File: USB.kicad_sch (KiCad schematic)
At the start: 44 parts, among them J3 USB_C_Receptacle_USB2.0, J4 USB_A_Stacked, U2 CP2102N-Axx-xQFN20, U3 FSUSB42MUX, U4 FSUSB42MUX, U5 TPD4EUSB30, U6 USB2422, U7 AP2171W, U8 TPD4EUSB30, Y1 24MHz

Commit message: Use HRO USB-C part number to match footprint
The footprint is not compatible with the JAE part. Specify the HRO USB-C
part number instead.

Fixes: #14

Signed-off-by: Stefan Agner <stefan@agner.ch>
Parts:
- J3: Manufacturer JAE -> HRO; PartNumber DX07S016JA3R1500 -> TYPE-C-31-M-12
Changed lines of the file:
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@@
       (effects (font (size 1.27 1.27)) hide)
     )
-    (property "Manufacturer" "JAE" (id 4) (at 153.67 140.97 0)
+    (property "Manufacturer" "HRO" (id 4) (at 153.67 140.97 0)
       (effects (font (size 1.27 1.27)) hide)
     )
-    (property "PartNumber" "DX07S016JA3R1500" (id 5) (at 153.67 140.97 0)
+    (property "PartNumber" "TYPE-C-31-M-12" (id 5) (at 153.67 140.97 0)
       (effects (font (size 1.27 1.27)) hide)
     )

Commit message: Fix CP2102N footprint
Choose Silicon Labs specific QFN20 footprint.

Signed-off-by: Stefan Agner <stefan@agner.ch>
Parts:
- U2: footprint Package_DFN_QFN:SiliconLabs_QFN-20-1EP_3x3mm_P0.5mm -> Package_DFN_QFN:SiliconLabs_QFN-20-1EP_3x3mm_P0.5mm_EP1.8x1.8mm
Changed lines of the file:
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@@
     (property "Reference" "U2" (id 0) (at 35.56 160.655 0))
     (property "Value" "CP2102N-Axx-xQFN20" (id 1) (at 58.42 160.655 0))
-    (property "Footprint" "Package_DFN_QFN:SiliconLabs_QFN-20-1EP_3x3mm_P0.5mm" (id 2) (at 77.47 160.655 0)
+    (property "Footprint" "Package_DFN_QFN:SiliconLabs_QFN-20-1EP_3x3mm_P0.5mm_EP1.8x1.8mm" (id 2) (at 77.47 160.655 0)
       (effects (font (size 1.27 1.27)) hide)
     )

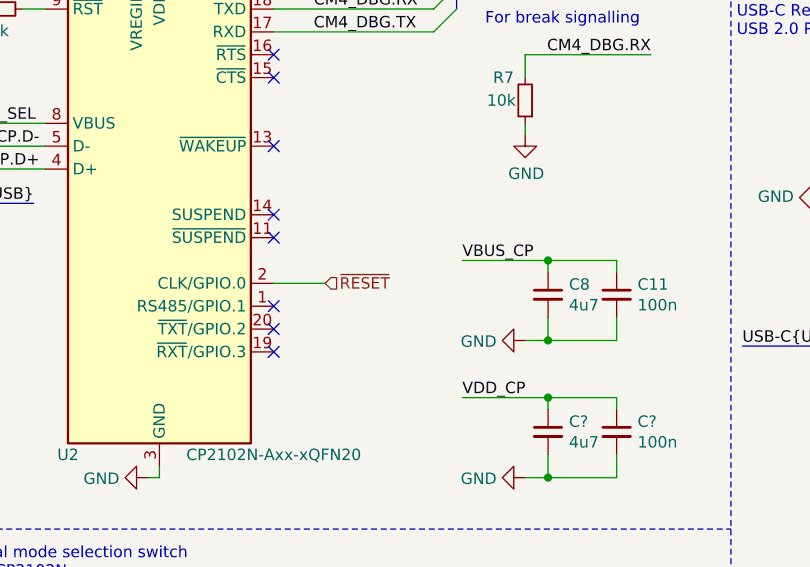
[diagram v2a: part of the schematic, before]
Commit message: Redesign buttons/switches
Remove power/reset/recovery switch. Power and reset is not really required
and recovery mode (USB Boot) can be triggered via jumper. Make the Fan
and RPiLED a new separate config so we can leave them unpopulated. Add a
second GPIO controlled switch.

Fixes: #16

Signed-off-by: Stefan Agner <stefan@agner.ch>
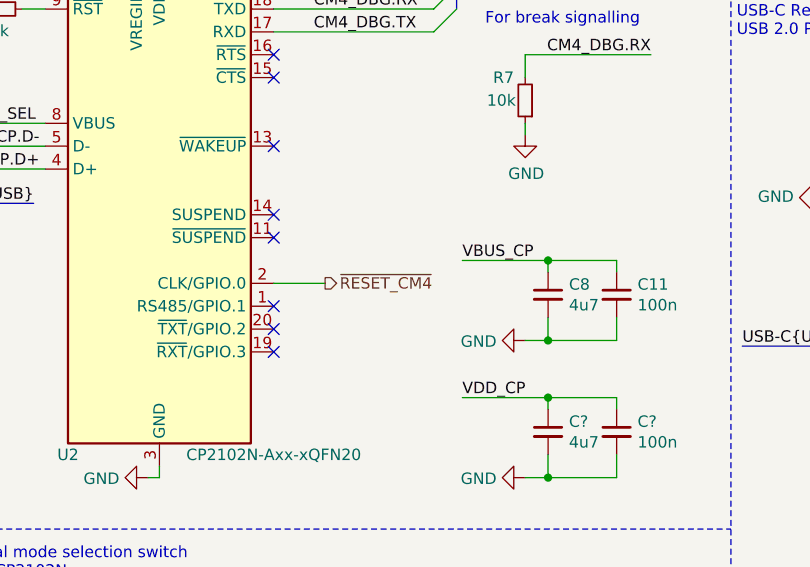
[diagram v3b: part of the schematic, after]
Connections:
- net ~RESET renamed ~RESET_CM4
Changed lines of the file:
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@@
     (comment 2 "Light Blue")
   )
+  (bus_alias "I2C" (members "SDA" "SCL"))
+  (bus_alias "USB" (members "D+" "D-"))
   (bus_alias "CM4_USB" (members "CM4_USB_D+" "CM4_USB_D-" "CM4_USB_OTG_ID"))
-  (bus_alias "USB" (members "D+" "D-"))
-  (bus_alias "I2C" (members "SDA" "SCL"))
   (junction (at 22.86 80.01) (diameter 0.9144) (color 0 0 0 0))
   (junction (at 22.86 88.9) (diameter 0.9144) (color 0 0 0 0))
@@
     (effects (font (size 1.27 1.27)) (justify right))
   )
-  (hierarchical_label "~RESET" (shape input) (at 64.135 141.605 0)
+  (hierarchical_label "~RESET_CM4" (shape output) (at 64.135 141.605 0)
     (effects (font (size 1.27 1.27)) (justify left))
   )
@@
   (symbol (lib_id "power:GND") (at 86.36 147.955 270) (unit 1)
     (in_bom yes) (on_board yes)
-    (property "Reference" "#PWR?" (id 0) (at 80.01 147.955 0)
+    (property "Reference" "#PWR0191" (id 0) (at 80.01 147.955 0)
       (effects (font (size 1.27 1.27)) hide)
     )
@@
   (symbol (lib_id "power:GND") (at 86.36 163.195 270) (unit 1)
     (in_bom yes) (on_board yes)
-    (property "Reference" "#PWR?" (id 0) (at 80.01 163.195 0)
+    (property "Reference" "#PWR0192" (id 0) (at 80.01 163.195 0)
       (effects (font (size 1.27 1.27)) hide)
     )
@@
   (symbol (lib_id "power:GND") (at 103.505 75.565 270) (unit 1)
     (in_bom yes) (on_board yes)
-    (property "Reference" "#PWR?" (id 0) (at 97.155 75.565 0)
-      (effects (font (size 1.27 1.27)) hide)
-    )
+    (property "Reference" "#PWR0193" (id 0) (at 97.155 75.565 0)
+      (effects (font (size 1.27 1.27)) hide)
+    )

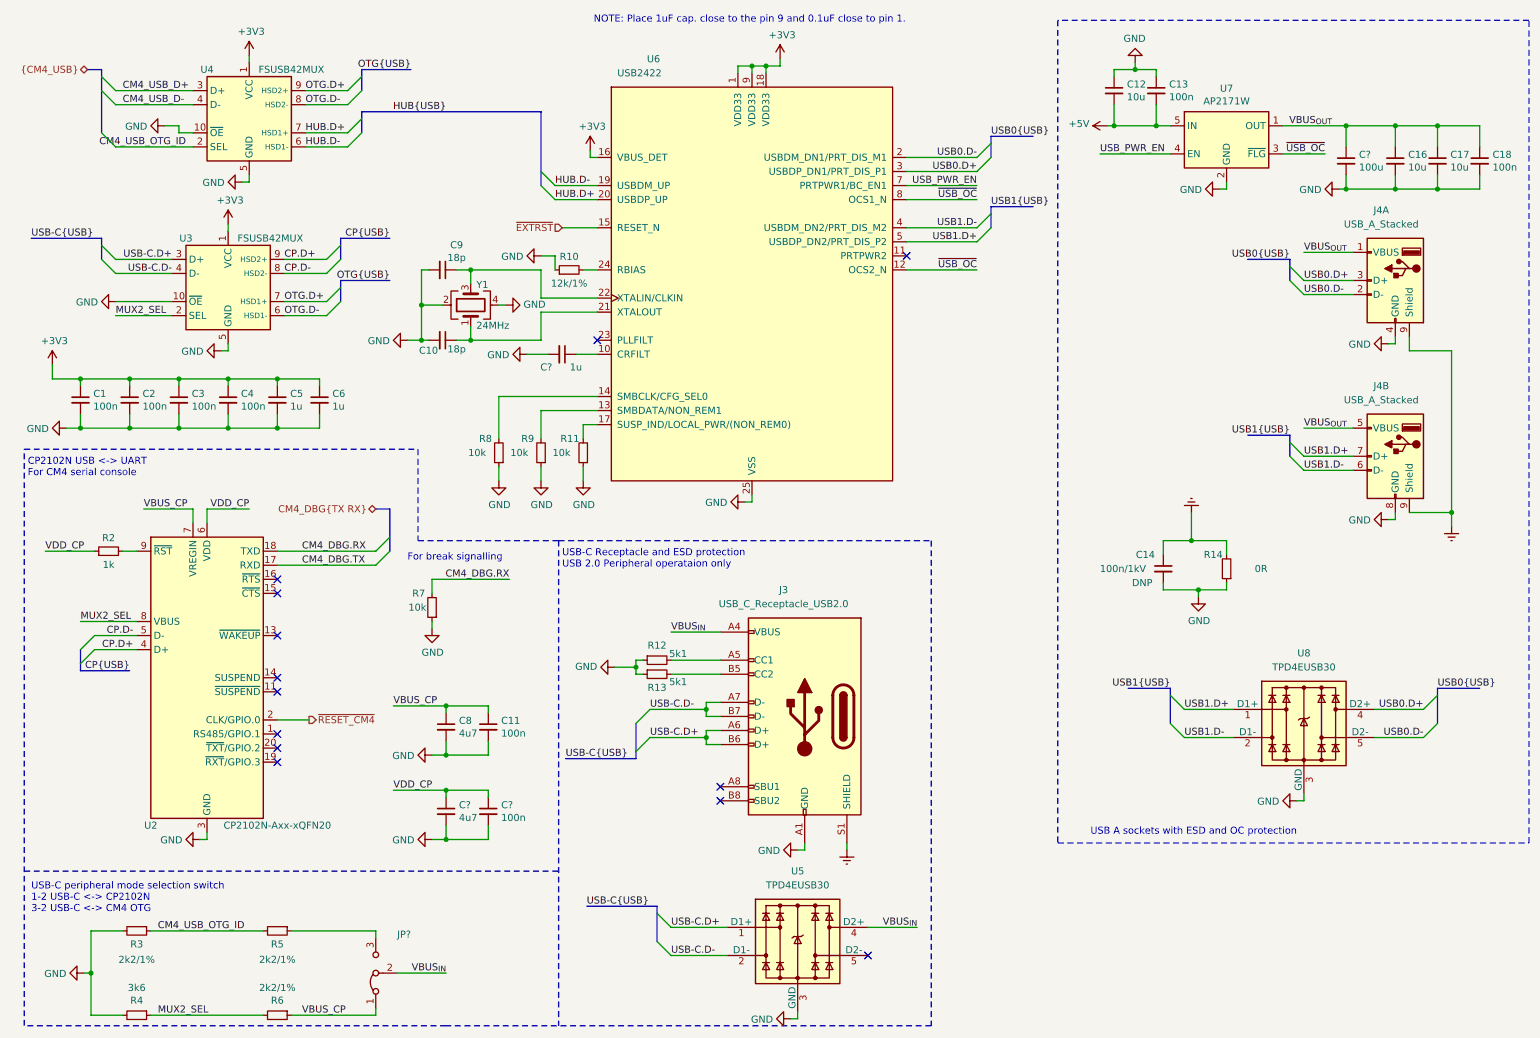
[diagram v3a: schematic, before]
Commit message: Assign footprints and annotate components
Signed-off-by: Stefan Agner <stefan@agner.ch>
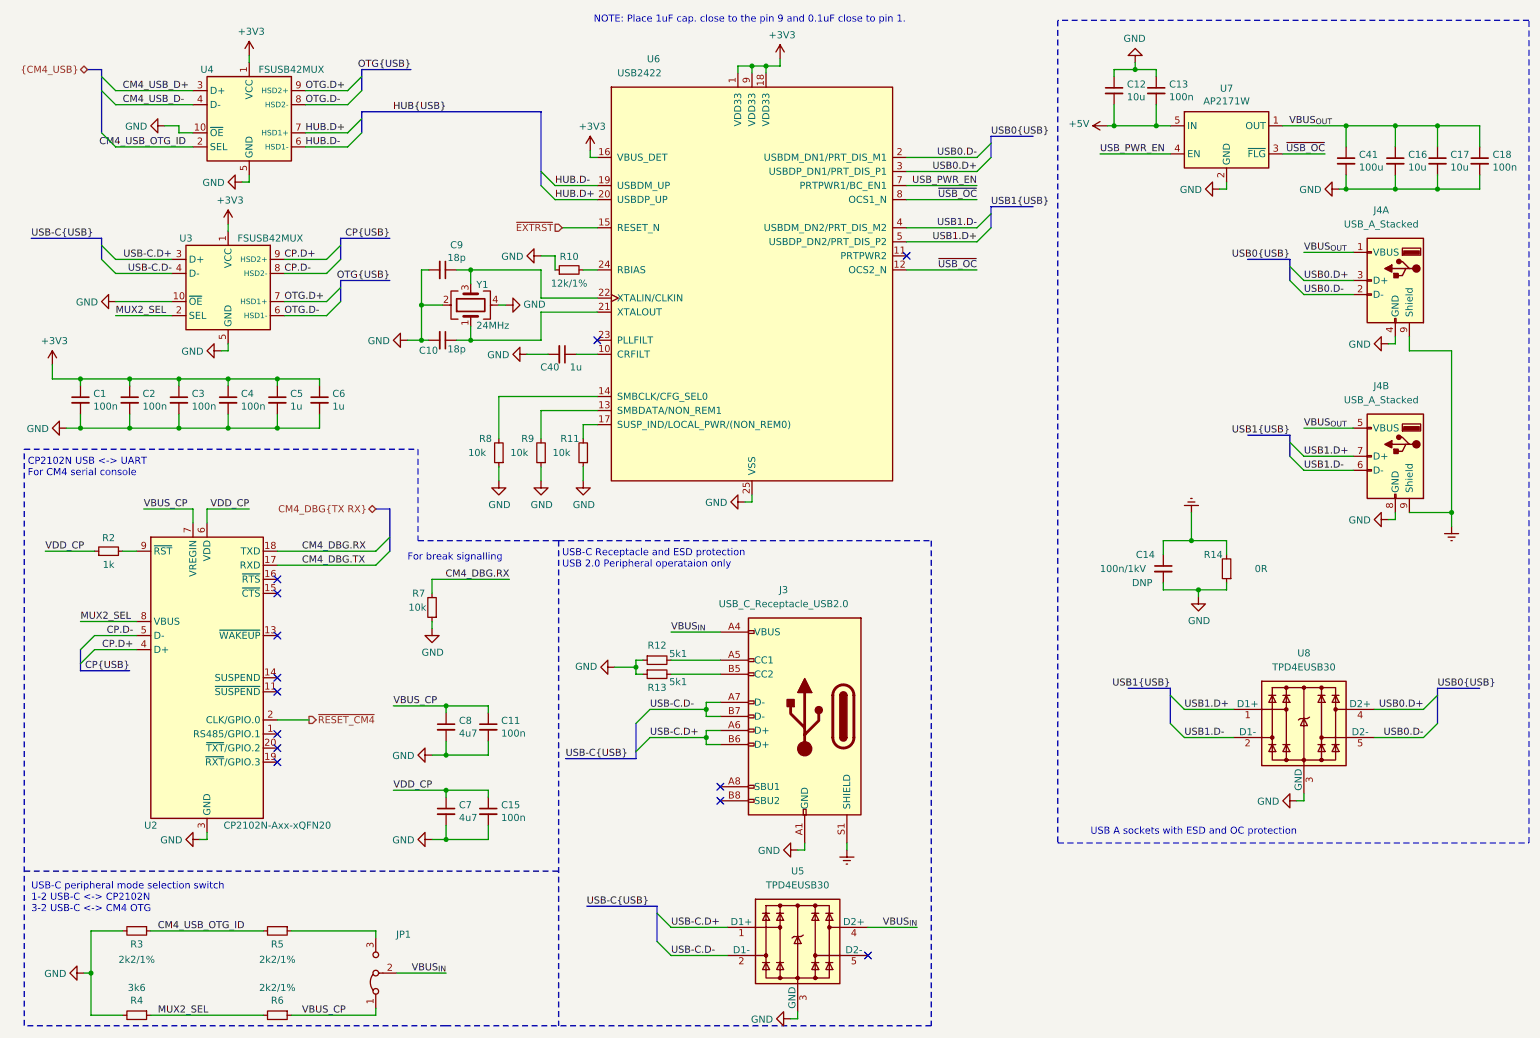
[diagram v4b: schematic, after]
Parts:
- JP1: renamed from JP?; footprint (none) -> Connector_PinHeader_2.54mm:PinHeader_1x03_P2.54mm_Vertical
- gave numbers to parts that had none: 4
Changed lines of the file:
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@@
     (comment 2 "Light Blue")
   )
+  (bus_alias "CM4_USB" (members "CM4_USB_D+" "CM4_USB_D-" "CM4_USB_OTG_ID"))
+  (bus_alias "USB" (members "D+" "D-"))
   (bus_alias "I2C" (members "SDA" "SCL"))
-  (bus_alias "USB" (members "D+" "D-"))
-  (bus_alias "CM4_USB" (members "CM4_USB_D+" "CM4_USB_D-" "CM4_USB_OTG_ID"))
   (junction (at 22.86 80.01) (diameter 0.9144) (color 0 0 0 0))
   (junction (at 22.86 88.9) (diameter 0.9144) (color 0 0 0 0))
@@
   (symbol (lib_id "Device:C_Small") (at 88.9 158.115 0) (unit 1)
     (in_bom yes) (on_board yes)
-    (property "Reference" "C?" (id 0) (at 91.2242 156.9656 0)
+    (property "Reference" "C7" (id 0) (at 91.2242 156.9656 0)
       (effects (font (size 1.27 1.27)) (justify left))
     )
@@
   (symbol (lib_id "Device:C_Small") (at 96.52 158.115 0) (unit 1)
     (in_bom yes) (on_board yes)
-    (property "Reference" "C?" (id 0) (at 98.8442 156.9656 0)
+    (property "Reference" "C15" (id 0) (at 98.8442 156.9656 0)
       (effects (font (size 1.27 1.27)) (justify left))
     )
@@
   (symbol (lib_id "Device:C_Small") (at 109.855 75.565 270) (unit 1)
     (in_bom yes) (on_board yes)
-    (property "Reference" "C?" (id 0) (at 105.9244 77.8892 90)
+    (property "Reference" "C40" (id 0) (at 105.9244 77.8892 90)
       (effects (font (size 1.27 1.27)) (justify left))
     )
@@
   (symbol (lib_id "Device:C_Small") (at 251.46 40.64 0) (unit 1)
     (in_bom yes) (on_board yes)
-    (property "Reference" "C?" (id 0) (at 253.7842 39.4906 0)
+    (property "Reference" "C41" (id 0) (at 253.7842 39.4906 0)
       (effects (font (size 1.27 1.27)) (justify left))
     )
@@
   (symbol (lib_id "Jumper:Jumper_3_Bridged12") (at 76.2 187.325 90) (unit 1)
     (in_bom yes) (on_board yes)
-    (property "Reference" "JP?" (id 0) (at 82.55 180.3399 90)
+    (property "Reference" "JP1" (id 0) (at 82.55 180.3399 90)
       (effects (font (size 1.27 1.27)) (justify left))
     )
@@
       (effects (font (size 1.27 1.27)) (justify left) hide)
     )
-    (property "Footprint" "" (id 2) (at 76.2 187.325 0)
-      (effects (font (size 1.27 1.27)) hide)
-    )
+    (property "Footprint" "Connector_PinHeader_2.54mm:PinHeader_1x03_P2.54mm_Vertical" (id 2) (at 76.2 187.325 0)
+      (effects (font (size 1.27 1.27)) hide)
+    )

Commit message: Adjust Manufacturer/PartNumber for some parts
- Use Diodes B2100-13-F consistently
- Define part for pin headers
- Replace N-Channel MOSFET for PoE with BSZ440N10NS3GATMA1
- Define Input protection MOSFET DMP3013SFV-7

Signed-off-by: Stefan Agner <stefan@agner.ch>
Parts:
- JP1: Manufacturer (none) -> Adam Tech; PartNumber (none) -> PH1-03-UA
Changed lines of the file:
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@@
     (comment 2 "Light Blue")
   )
+  (bus_alias "I2C" (members "SDA" "SCL"))
+  (bus_alias "USB" (members "D+" "D-"))
   (bus_alias "CM4_USB" (members "CM4_USB_D+" "CM4_USB_D-" "CM4_USB_OTG_ID"))
-  (bus_alias "USB" (members "D+" "D-"))
-  (bus_alias "I2C" (members "SDA" "SCL"))
   (junction (at 22.86 80.01) (diameter 0.9144) (color 0 0 0 0))
   (junction (at 22.86 88.9) (diameter 0.9144) (color 0 0 0 0))
@@
       (effects (font (size 1.27 1.27)) hide)
     )
+    (property "Manufacturer" "Adam Tech" (id 4) (at 76.2 187.325 90)
+      (effects (font (size 1.27 1.27)) hide)
+    )
+    (property "PartNumber" "PH1-03-UA" (id 5) (at 76.2 187.325 90)
+      (effects (font (size 1.27 1.27)) hide)
+    )

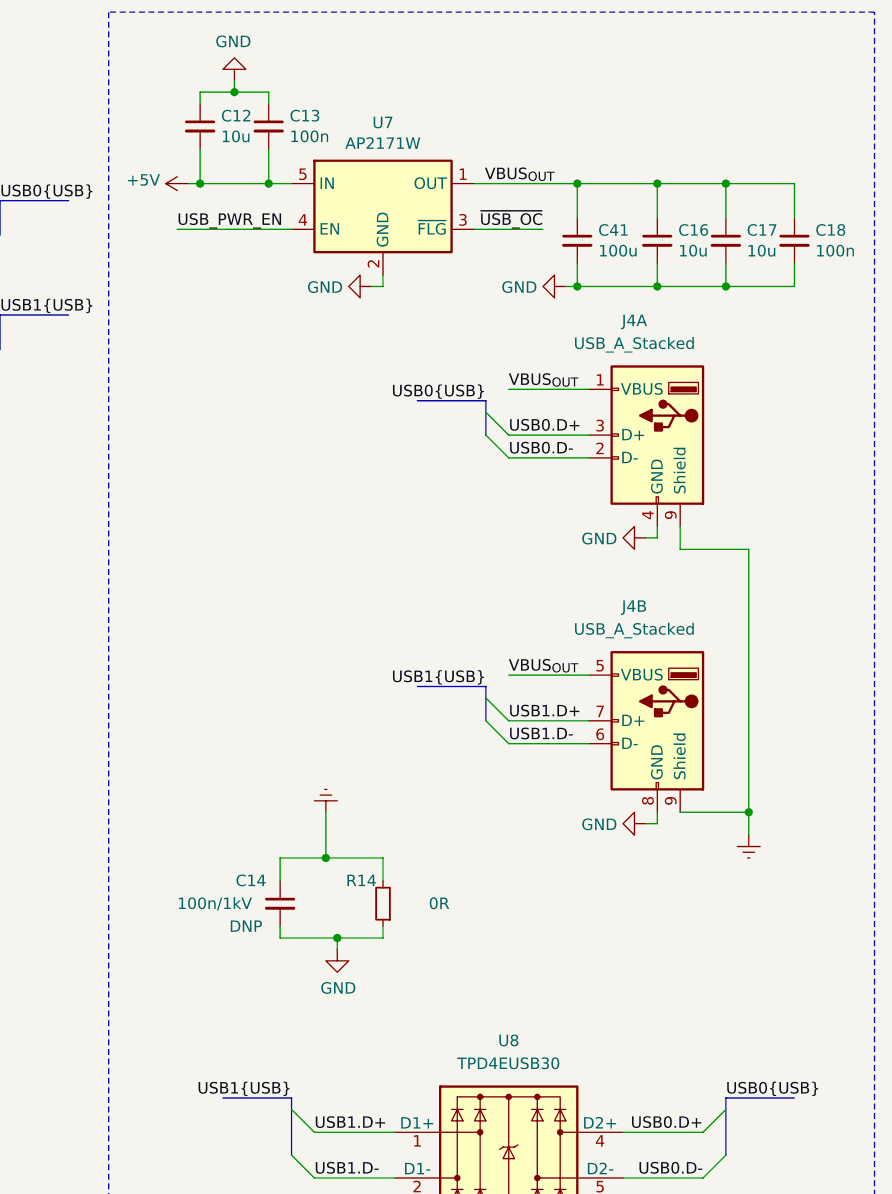
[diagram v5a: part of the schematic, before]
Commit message: Adjust various parts to improve BOM
- Replace unusual/high value ceramics with lower value in parallel
- Use the same protection Shottky Diode in PoE as in regular input
  (B340LB-13-F)
- Replace PoE rectifier Diodes with B1100-13-F
- Replace PoE Inductor (SRN6045TA-3R3Y) with the same part from 5V power
  supply (Taiyo Yuden NRS8030T3R3MJGJ)
- Correctly specify Pulse Electronics transformer

Signed-off-by: Stefan Agner <stefan@agner.ch>
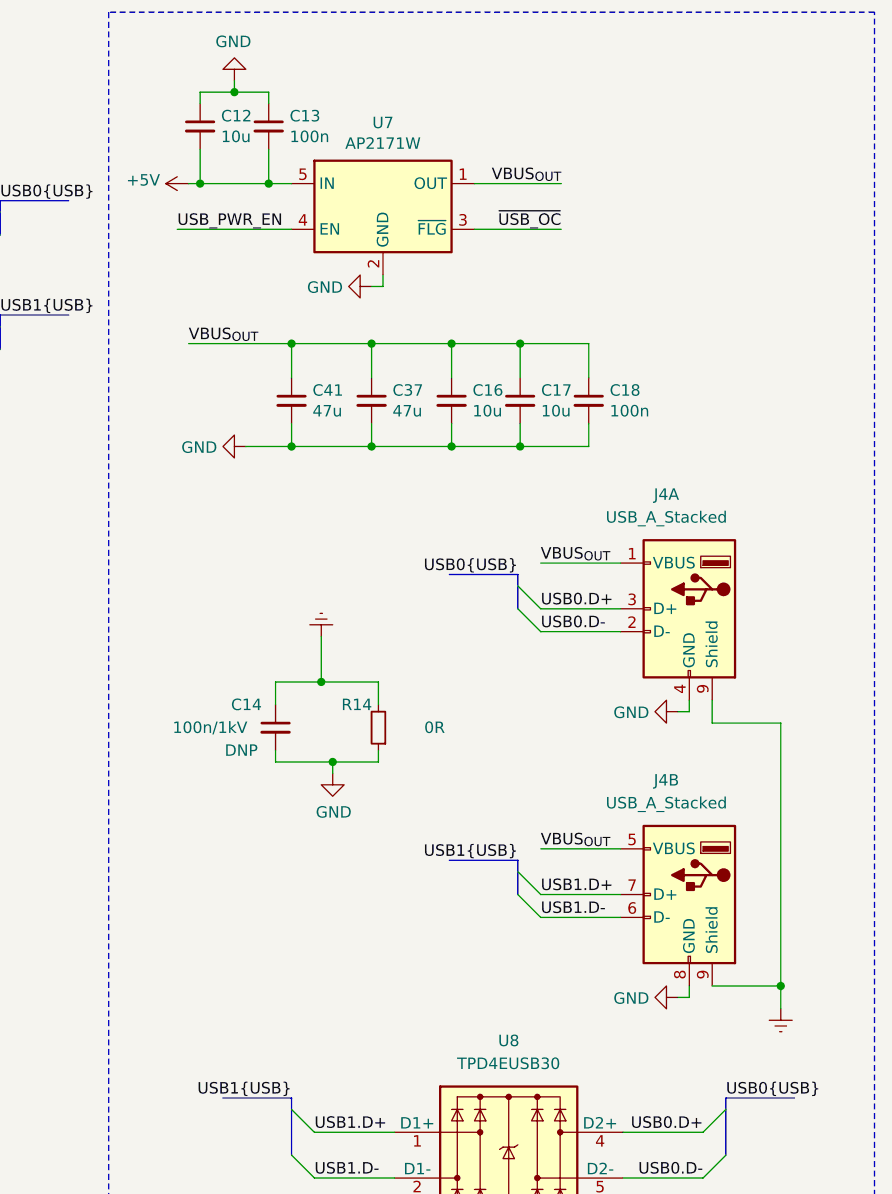
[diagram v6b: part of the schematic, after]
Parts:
- added C37: 47u, Capacitor_SMD:C_0805_2012Metric, symbol Device:C_Small
- C41: value 100u -> 47u
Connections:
- net GND: now also C37.2
- net VBUS_{OUT}: now also C37.1
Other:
- moved on the sheet: C14, C16, C17, C18, C41, J4A, J4B, R14
